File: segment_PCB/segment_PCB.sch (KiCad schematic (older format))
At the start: 147 parts, among them J1 USB_C_Receptacle_USB2.0, J2 AVR-ISP-6, SW1 SW_Push, SW11 SW_Push, SW12 SW_Push, SW13 SW_Push, SW14 SW_Push, SW15 SW_Push, SW16 SW_Push, SW17 SW_Push, SW18 SW_Push, SW19 SW_Push, SW2 SW_Push, SW20 SW_Push, SW22 SW_Push, SW23 SW_Push, SW24 SW_Push, SW25 SW_Push, SW26 SW_Push, SW27 SW_Push, SW28 SW_Push, SW29 SW_Push, SW3 SW_Push, SW30 SW_Push, SW32 SW_Push, SW33 SW_Push, SW34 SW_Push, SW35 SW_Push, SW36 SW_Push, SW37 SW_Push, SW38 SW_Push, SW39 SW_Push, SW4 SW_Push, SW40 SW_Push, SW42 SW_Push, SW43 SW_Push, SW44 SW_Push, SW45 SW_Push, SW46 SW_Push, SW47 SW_Push, SW48 SW_Push, SW49 SW_Push, SW5 SW_Push, SW50 SW_Push, SW52 SW_Push, SW53 SW_Push, SW54 SW_Push, SW55 SW_Push, SW56 SW_Push, SW57 SW_Push, SW58 SW_Push, SW6 SW_Push, SW61 SW_Push, SW62 SW_Push, SW64 SW_Push, SW65 SW_Push, SW66 SW_Push, SW67 SW_Push, SW68 SW_Push, SW7 SW_Push, SW71 SW_Push, SW8 SW_Push, SW9 SW_Push, U1 ATtiny2313A-PU, Y1 12MHz

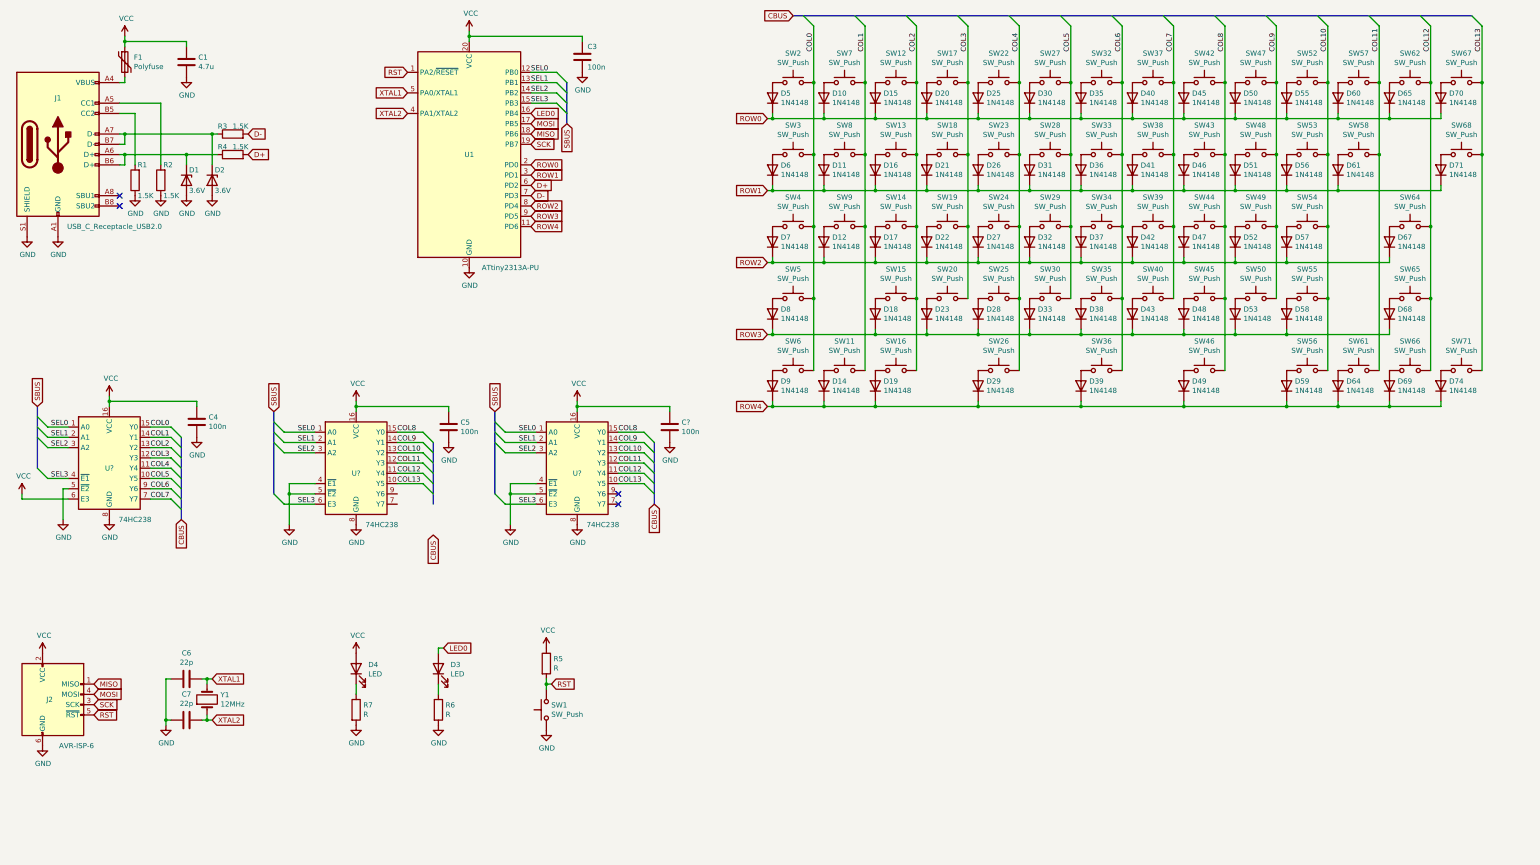
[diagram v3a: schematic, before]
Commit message: Fixed USB config; introduced '365 buffers in place of diodes
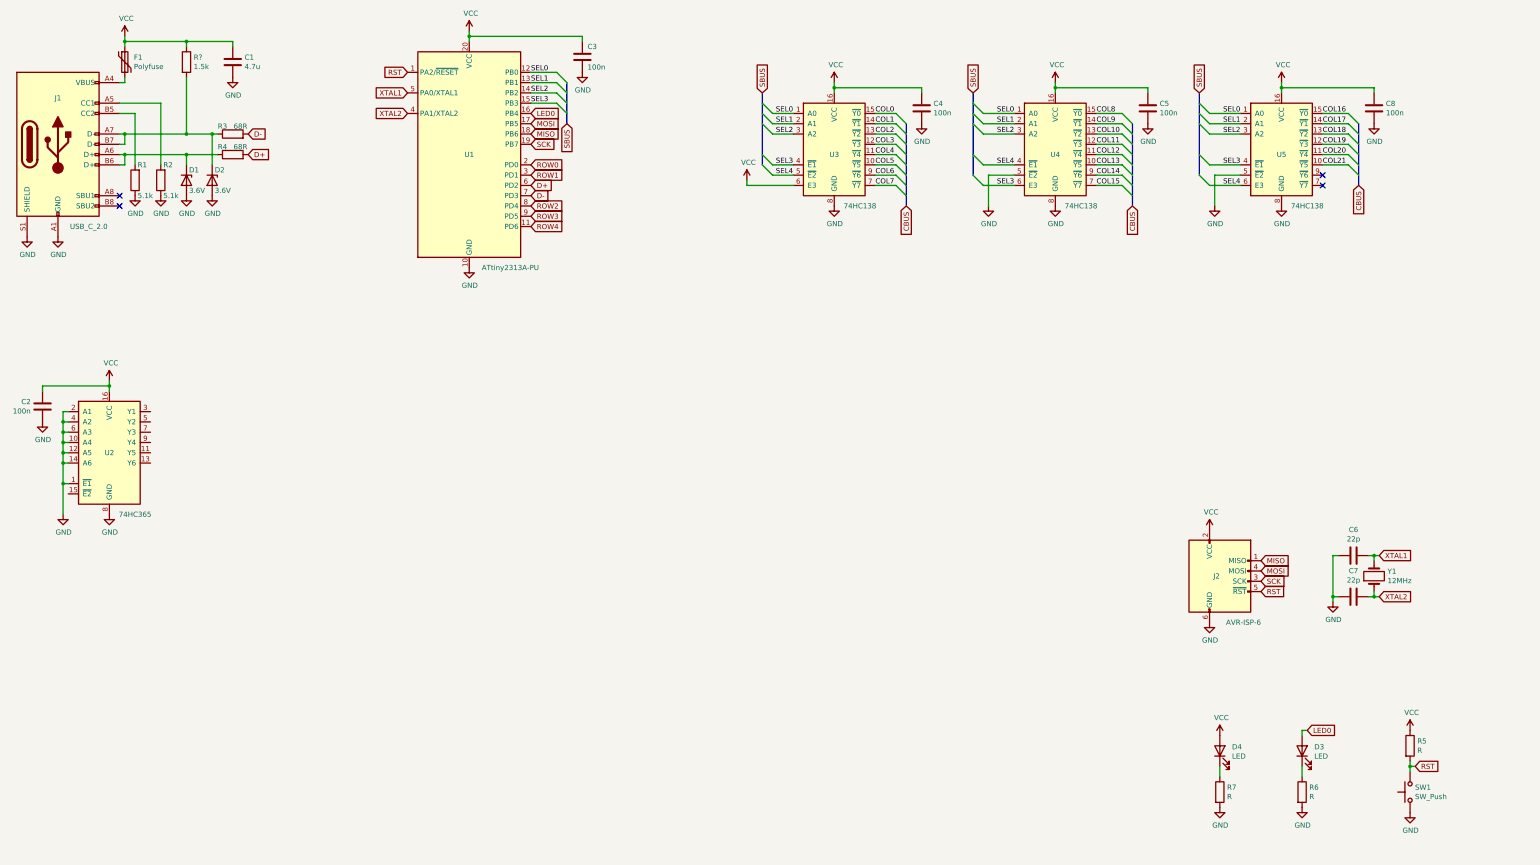
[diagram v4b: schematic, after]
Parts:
- removed D10, D11, D12, D14, D15, D16, D17, D18, D19, D20, D21, D22, D23, D25, D26, D27, D28, D29, D30, D31, D32, D33, D35, D36, D37, D38, D39, D40, D41, D42, D43, D45, D46, D47, D48, D49, D5, D50, D51, D52, D53, D55, D56, D57, D58, D59, D6, D60, D61, D64, D65, D67, D68, D69, D7, D70, D71, D74, D8, D9: 1N4148, symbol Device:D
- removed SW11, SW12, SW13, SW14, SW15, SW16, SW17, SW18, SW19, SW2, SW20, SW22, SW23, SW24, SW25, SW26, SW27, SW28, SW29, SW3, SW30, SW32, SW33, SW34, SW35, SW36, SW37, SW38, SW39, SW4, SW40, SW42, SW43, SW44, SW45, SW46, SW47, SW48, SW49, SW5, SW50, SW52, SW53, SW54, SW55, SW56, SW57, SW58, SW6, SW61, SW62, SW64, SW65, SW66, SW67, SW68, SW7, SW71, SW8, SW9: SW_Push, symbol Switch:SW_Push
- removed U? (x3): 74HC238, symbol Segment_Parts:74HC238
- added C2: 100n, Capacitor_THT:C_Disc_D3.0mm_W1.6mm_P2.50mm, symbol Device:C
- added R?: 1.5k, symbol Device:R
- added U2: 74HC365, symbol Segment_Parts:74HC365
- added U3, U4, U5: 74HC138, symbol Segment_Parts:74HC138
- J1: value USB_C_Receptacle_USB2.0 -> USB_C_2.0
- R1, R2: value 1.5K -> 5.1k
- R3, R4: value 1.5K -> 68R
- gave numbers to parts that had none: 1
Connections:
- net COL0: now also U3.15 (~Y0)
- net COL1: now also U3.14 (~Y1)
- net COL10: now also U4.13 (~Y2)
- net COL11: now also U4.12 (~Y3)
- net COL12: now also U4.11 (~Y4)
- net COL13: now also U4.10 (~Y5)
- net COL2: now also U3.13 (~Y2)
- net COL3: now also U3.12 (~Y3)
- net COL4: now also U3.11 (~Y4)
- net COL5: now also U3.10 (~Y5)
- net COL6: now also U3.9 (~Y6)
- net COL7: now also U3.7 (~Y7)
- net COL8: now also U4.15 (~Y0)
- net COL9: now also U4.14 (~Y1)
- net GND: now also C2.2, U2.1 (~E1), U2.10 (A4), U2.12 (A5), U2.14 (A6), U2.2 (A1), U2.4 (A2), U2.6 (A3), U2.8 (GND), U3.8 (GND), U4.5 (~E2), U4.8 (GND), U5.5 (~E2), U5.8 (GND)
- net SEL0: now also U3.1 (A0), U4.1 (A0), U5.1 (A0)
- net SEL1: now also U3.2 (A1), U4.2 (A1), U5.2 (A1)
- net SEL2: now also U3.3 (A2), U4.3 (A2), U5.3 (A2)
- net SEL3: now also U3.4 (~E1), U4.6 (E3), U5.4 (~E1)
- net VCC: now also C2.1, R?.1, U2.16 (VCC), U3.16 (VCC), U3.6 (E3), U4.16 (VCC), U5.16 (VCC)
- net at D2.1 (K), J1.A7 (D-), J1.B7 (D-)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: now also R?.2
- new net COL14: U4.9 (~Y6)
- new net COL15: U4.7 (~Y7)
- new net COL16: U5.15 (~Y0)
- new net COL17: U5.14 (~Y1)
- new net COL18: U5.13 (~Y2)
- new net COL19: U5.12 (~Y3)
- new net COL20: U5.11 (~Y4)
- new net COL21: U5.10 (~Y5)
- new net SEL4: U3.5 (~E2), U4.4 (~E1), U5.6 (E3)
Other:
- moved on the sheet: C1, C4, C5, C6, C7, C8, D3, D4, J2, R5, R6, R7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

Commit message: replaced USB-C with DE-9.
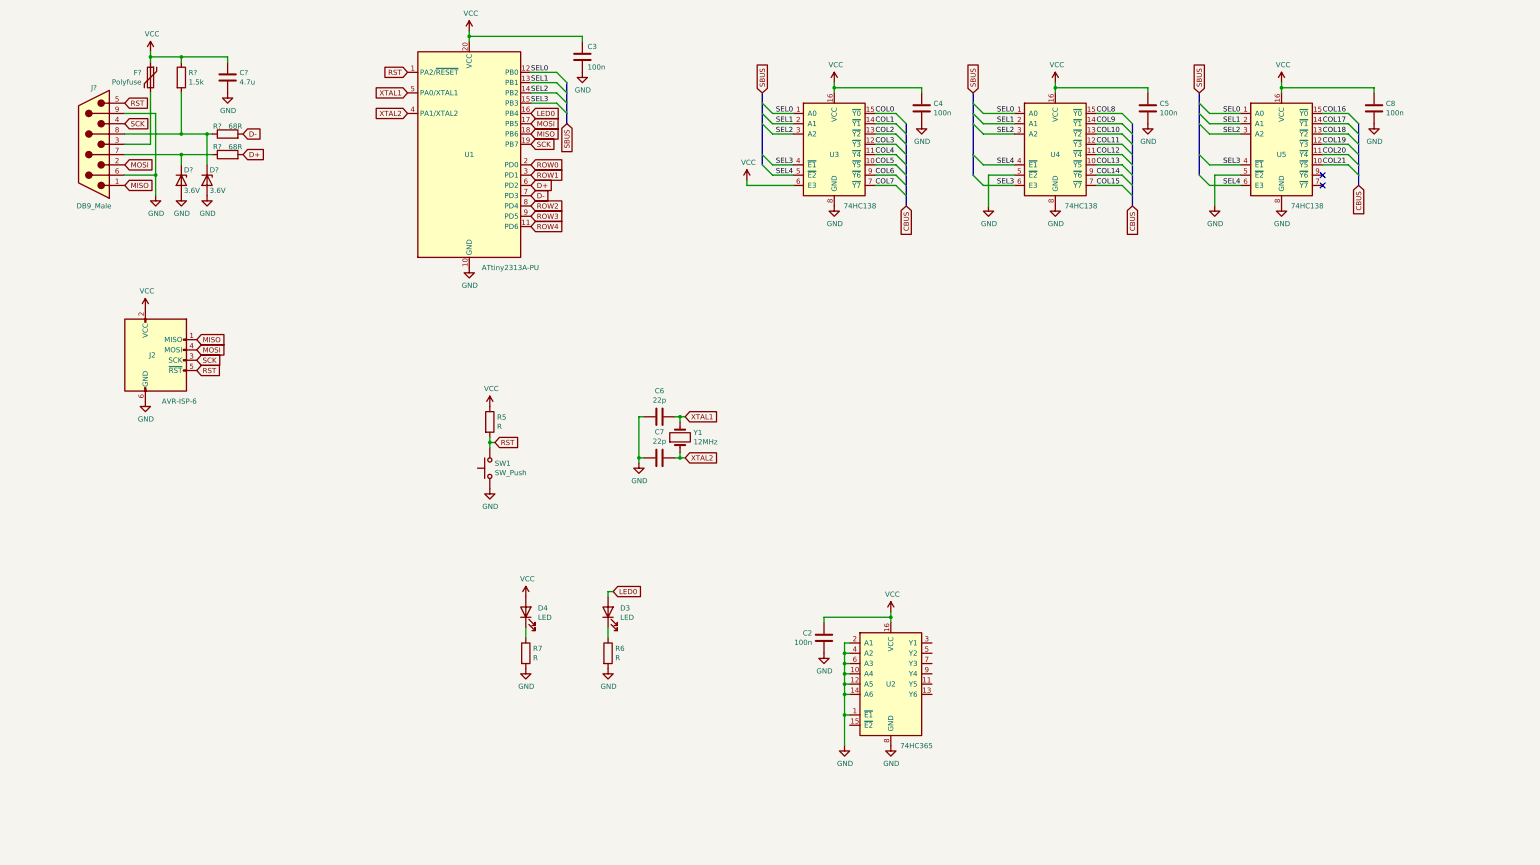
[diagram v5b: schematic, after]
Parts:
- removed C1: 4.7u, Capacitor_THT:C_Disc_D3.0mm_W1.6mm_P2.50mm, symbol Device:C
- removed D1, D2: 3.6V, Diode_THT:D_DO-35_SOD27_P7.62mm_Horizontal, symbol Device:D_Zener
- removed F1: Polyfuse, symbol Device:Polyfuse
- removed J1: USB_C_2.0, symbol Connector:USB_C_Receptacle_USB2.0
- removed R1, R2: 5.1k, Resistor_THT:R_Axial_DIN0204_L3.6mm_D1.6mm_P5.08mm_Horizontal, symbol Device:R
- removed R3, R4: 68R, Resistor_THT:R_Axial_DIN0204_L3.6mm_D1.6mm_P5.08mm_Horizontal, symbol Device:R
- removed R?: 1.5k, symbol Device:R
- added C?: 4.7u, Capacitor_THT:C_Disc_D3.0mm_W1.6mm_P2.50mm, symbol Device:C
- added D? (x2): 3.6V, Diode_THT:D_DO-35_SOD27_P7.62mm_Horizontal, symbol Device:D_Zener
- added F?: Polyfuse, symbol Device:Polyfuse
- added J?: DB9_Male, symbol Connector:DB9_Male
- added R? (x2): 68R, Resistor_THT:R_Axial_DIN0204_L3.6mm_D1.6mm_P5.08mm_Horizontal, symbol Device:R
- added R?: 1.5k, symbol Device:R
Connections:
- net D+: now also R?.2
- net D-: now also R?.2
- net GND: now also C?.2, D?.2 (A), D?.2 (A), J?.6, J?.9
- net MISO: now also J?.1
- net MOSI: now also J?.2
- net RST: now also J?.5
- net SCK: now also J?.4
- net VCC: now also C?.1, F?.1, R?.1
- new net: F?.2, J?.3
- new net: D?.1 (K), J?.7, R?.1
- new net: D?.1 (K), J?.8, R?.1, R?.2
- no-connect marks 4 -> 2
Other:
- moved on the sheet: C2, C6, C7, D3, D4, J2, R5, R6, R7, SW1, U2, Y1

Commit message: Added ATmega328P
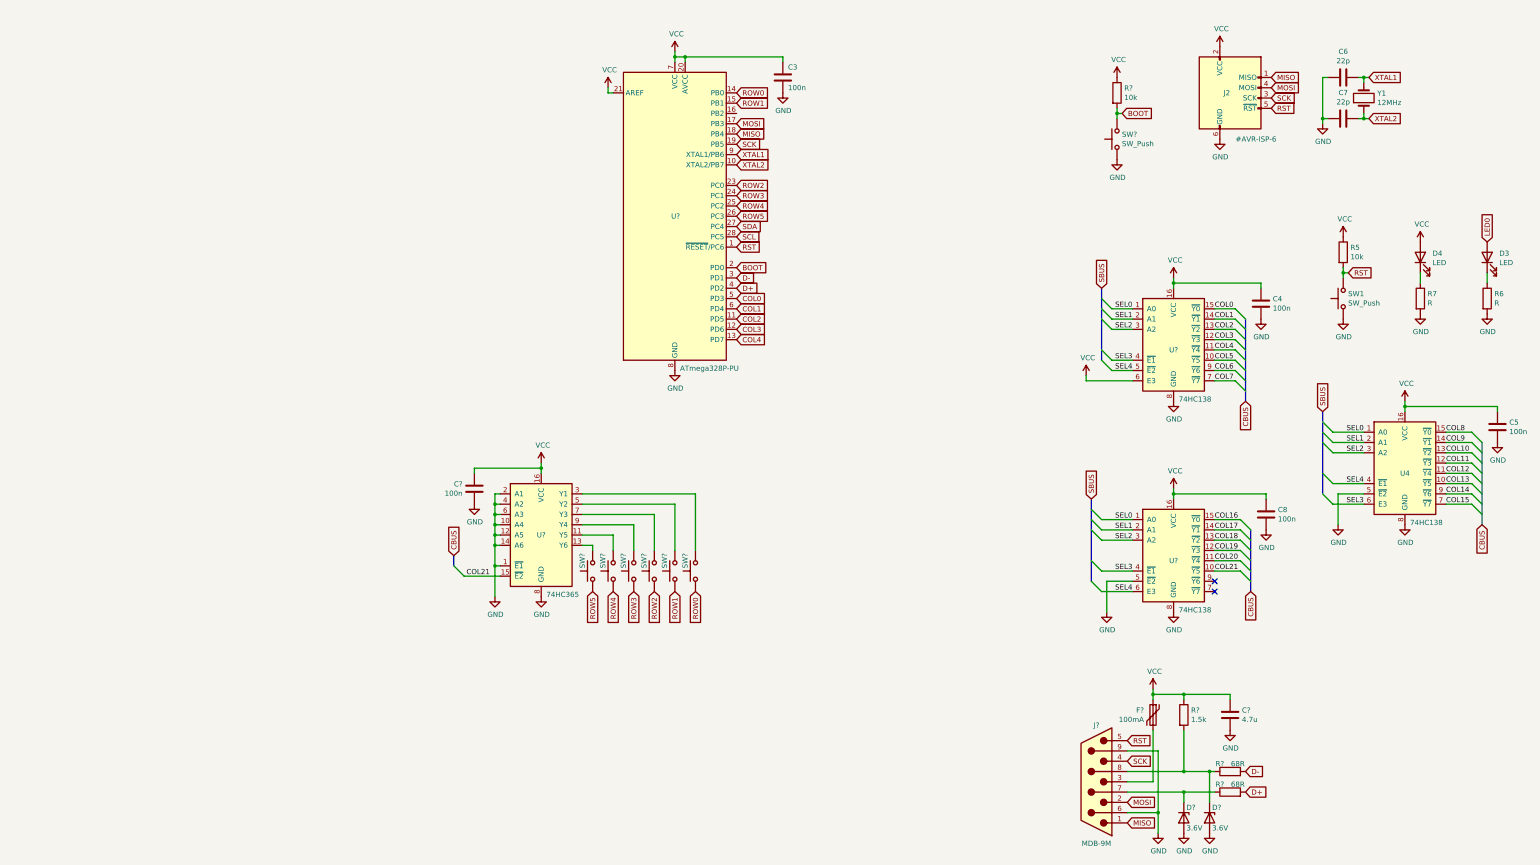
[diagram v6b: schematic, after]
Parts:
- removed C2: 100n, Capacitor_THT:C_Disc_D3.0mm_W1.6mm_P2.50mm, symbol Device:C
- removed U1: ATtiny2313A-PU, Package_DIP:DIP-20_W7.62mm, symbol MCU_Microchip_ATtiny:ATtiny2313A-PU
- removed U2: 74HC365, symbol Segment_Parts:74HC365
- removed U3, U5: 74HC138, symbol Segment_Parts:74HC138
- added C?: 100n, Capacitor_THT:C_Disc_D3.0mm_W1.6mm_P2.50mm, symbol Device:C
- added R?: 10k, Resistor_THT:R_Axial_DIN0204_L3.6mm_D1.6mm_P5.08mm_Horizontal, symbol Device:R
- added SW? (x7): SW_Push, symbol Switch:SW_Push
- added U? (x2): 74HC138, symbol Segment_Parts:74HC138
- added U?: ATmega328P-PU, Package_DIP:DIP-28_W7.62mm, symbol MCU_Microchip_ATmega:ATmega328P-PU
- added U?: 74HC365, symbol Segment_Parts:74HC365
- F?: value Polyfuse -> 100mA
- J2: value AVR-ISP-6 -> #AVR-ISP-6
- J?: value DB9_Male -> MDB-9M
- R5: value R -> 10k
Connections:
- net COL0: now also U?.15 (~Y0), U?.5 (PD3)
- net COL1: now also U?.14 (~Y1), U?.6 (PD4)
- net COL16: now also U?.15 (~Y0)
- net COL17: now also U?.14 (~Y1)
- net COL18: now also U?.13 (~Y2)
- net COL19: now also U?.12 (~Y3)
- net COL2: now also U?.11 (PD5), U?.13 (~Y2)
- net COL20: now also U?.11 (~Y4)
- net COL21: now also U?.10 (~Y5), U?.15 (~E2)
- net COL3: now also U?.12 (PD6), U?.12 (~Y3)
- net COL4: now also U?.11 (~Y4), U?.13 (PD7)
- net COL5: now also U?.10 (~Y5)
- net COL6: now also U?.9 (~Y6)
- net COL7: now also U?.7 (~Y7)
- net D+: now also U?.4 (PD2)
- net D-: now also U?.3 (PD1)
- net GND: now also C?.2, SW?.1, U?.1 (~E1), U?.10 (A4), U?.12 (A5), U?.14 (A6), U?.2 (A1), U?.22 (GND), U?.4 (A2), U?.5 (~E2), U?.6 (A3), U?.8 (GND), U?.8 (GND), U?.8 (GND), U?.8 (GND)
- net MISO: now also U?.18 (PB4)
- net MOSI: now also U?.17 (PB3)
- net ROW0: now also SW?.1, U?.14 (PB0)
- net ROW1: now also SW?.1, U?.15 (PB1)
- net ROW2: now also SW?.1, U?.23 (PC0)
- net ROW3: now also SW?.1, U?.24 (PC1)
- net ROW4: now also SW?.1, U?.25 (PC2)
- net RST: now also U?.1 (~RESET~/PC6)
- net SCK: now also U?.19 (PB5)
- net SEL0: now also U?.1 (A0), U?.1 (A0)
- net SEL1: now also U?.2 (A1), U?.2 (A1)
- net SEL2: now also U?.3 (A2), U?.3 (A2)
- net SEL3: now also U?.4 (~E1), U?.4 (~E1)
- net SEL4: now also U?.5 (~E2), U?.6 (E3)
- net VCC: now also C?.1, R?.1, U?.16 (VCC), U?.16 (VCC), U?.16 (VCC), U?.20 (AVCC), U?.21 (AREF), U?.6 (E3), U?.7 (VCC)
- net XTAL1: now also U?.9 (XTAL1/PB6)
- net XTAL2: now also U?.10 (XTAL2/PB7)
- new net: SW?.2, U?.11 (Y5)
- new net: SW?.2, U?.13 (Y6)
- new net: SW?.2, U?.3 (Y1)
- new net: SW?.2, U?.5 (Y2)
- new net: SW?.2, U?.7 (Y3)
- new net: SW?.2, U?.9 (Y4)
- new net BOOT: R?.2, SW?.2, U?.2 (PD0)
- new net ROW5: SW?.1, U?.26 (PC3)
- new net SCL: U?.28 (PC5)
- new net SDA: U?.27 (PC4)
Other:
- moved on the sheet: C3, C4, C5, C6, C7, C8, C?, D3, D4, D?, F?, J2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
